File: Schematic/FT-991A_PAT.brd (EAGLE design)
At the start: 44.6 x 59.8 mm, 38 parts, among them Q1 PE4259, Q2 MC78L09, Q3 DG2001, Q5 NCP553, Q7 J310, Q8 BFR193F, X1 IF_IN, X2 SCP_OUT, X3 SDR_OUT

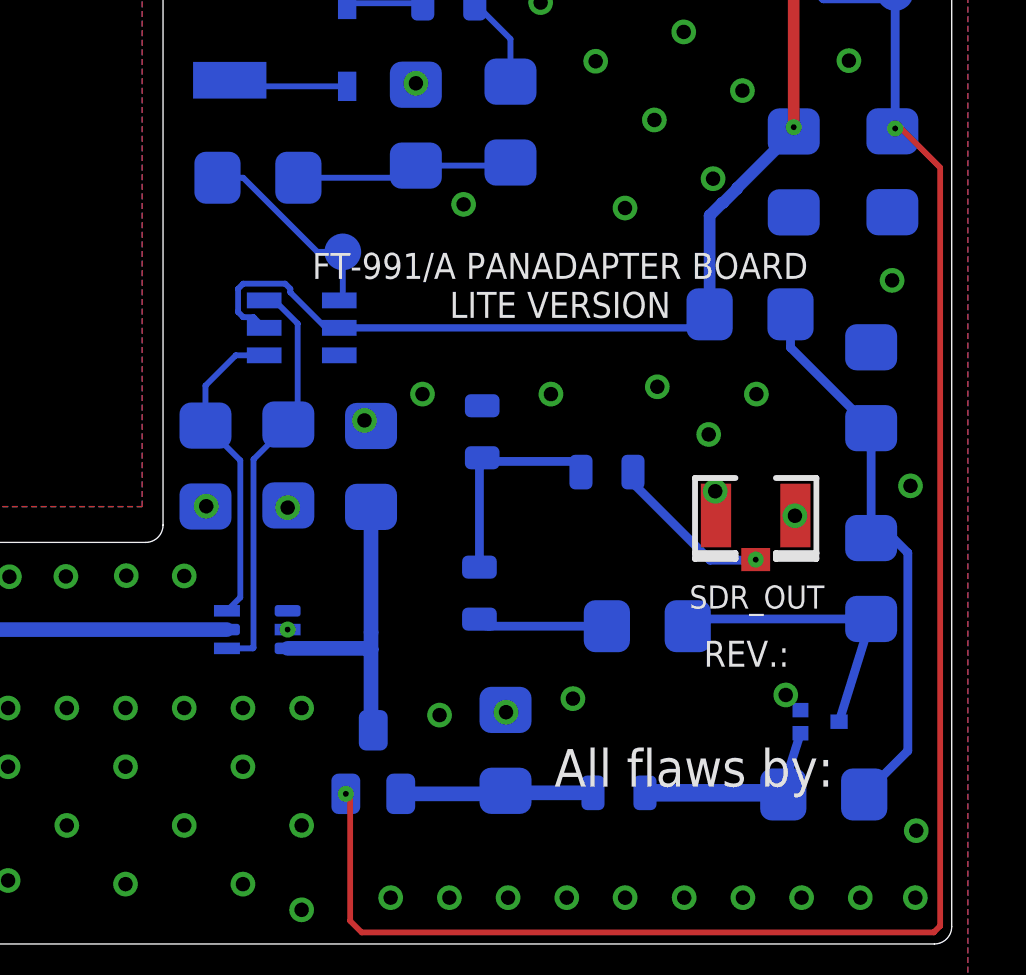
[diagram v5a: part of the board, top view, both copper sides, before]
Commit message: Updating Schematic and Board
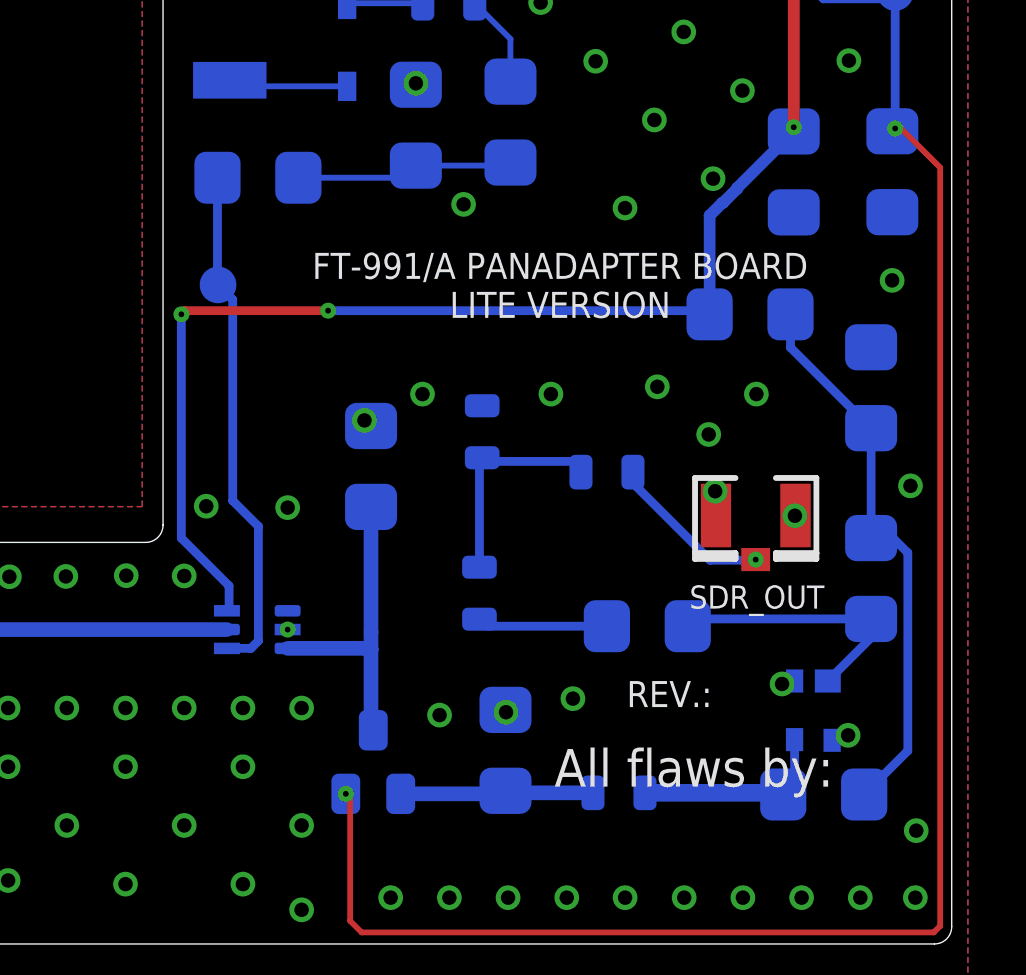
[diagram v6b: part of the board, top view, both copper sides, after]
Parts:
- removed Q3: DG2001, aarf:SOT23-6
- removed R1, R6: 100kΩ, aarf:1206
- Q8: value BFR193F -> BFP460; device aarf:TSFP-3 -> aarf:SOT343R
- moved TP3 4.47 mm to (25.5, 53.2)
- moved Q8 0.46 mm to (46.1, 38.5)
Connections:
- removed net NC: Q1.6, Q3.4, R1.2
- removed net NO: Q1.4, Q3.6, R6.2
- net 3V: now also Q1.6; no longer Q3.2, Q3.5
- net GNDA: now also Q8.1, Q8.3; no longer Q3.3, Q8.2, R1.1, R6.1
- net N$7: now also Q1.4; no longer Q3.1
- net ST2IN: now also Q8.4; no longer Q8.1
- net ST2OUT: now also Q8.2; no longer Q8.3
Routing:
- net NO: track 14.3 -> 0.00 mm
- net NC: track 11.0 -> 0.00 mm
- net 3V: track 43.2 -> 54.0 mm, vias 2 -> 4
- net N$7: track 7.14 -> 17.8 mm
- net ST2OUT: track 10.6 -> 9.62 mm

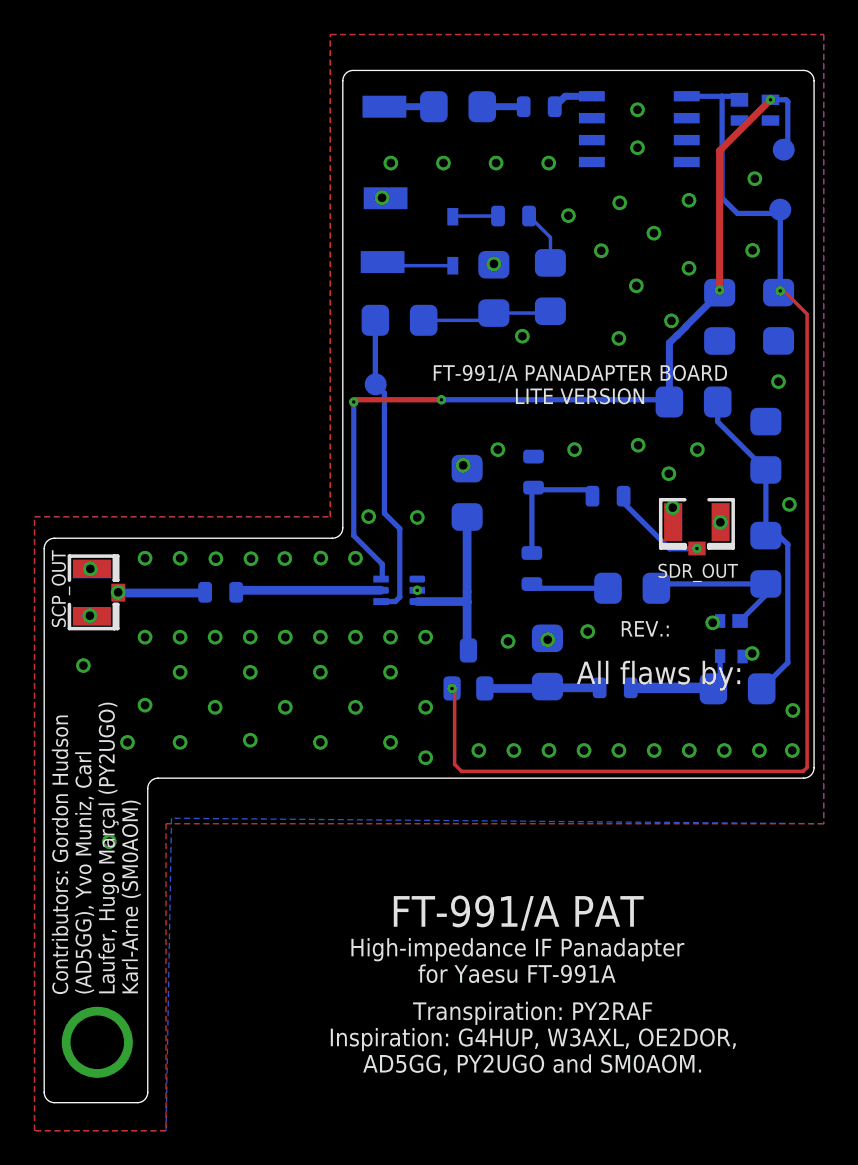
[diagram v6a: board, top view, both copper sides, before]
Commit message: Revision V: Improvements
* Improved BFP460 and NCP553 footprint
* Some routing  and CPW improvements
* Rebasing the library to the latest
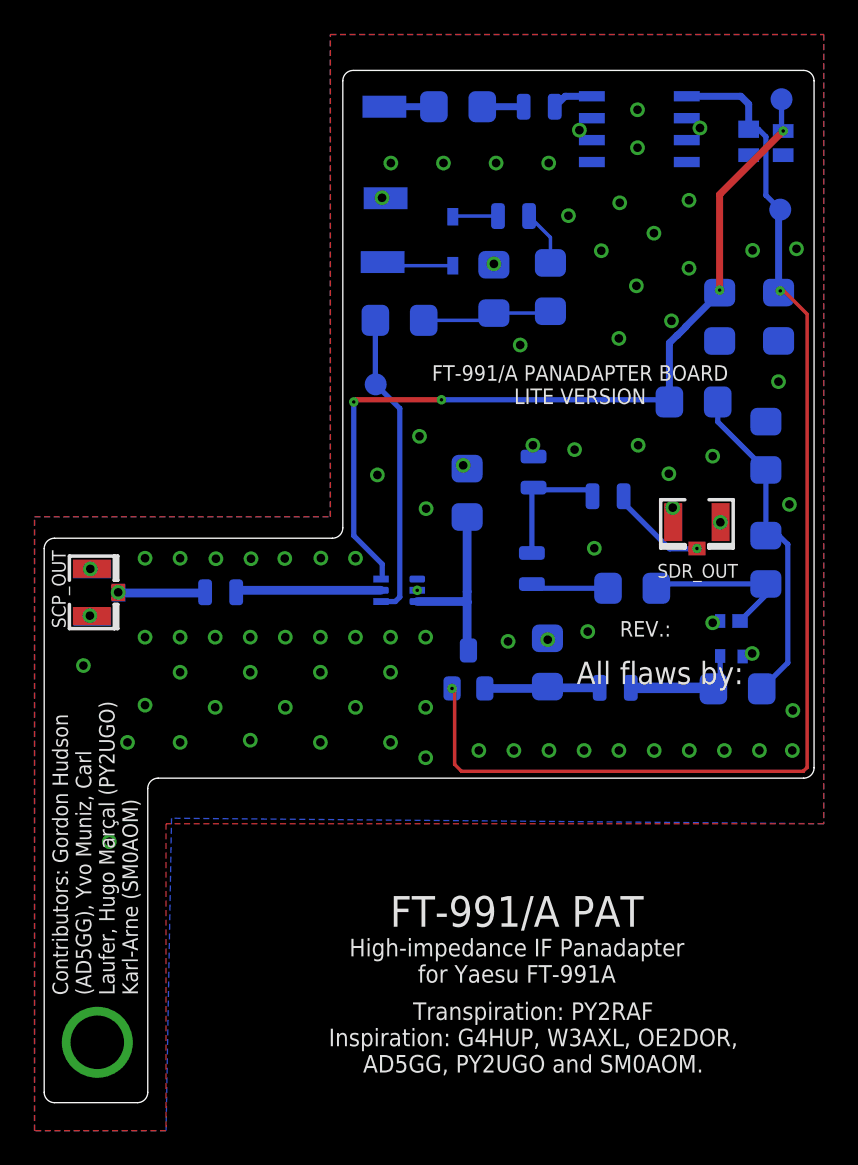
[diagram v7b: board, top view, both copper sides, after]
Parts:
- moved TP2 2.92 mm to (49.0, 69.7)
- moved Q5 2.01 mm to (48.1, 67.2)
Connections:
- net N$18 renamed TX9
- net N$7 renamed SW_FLIP
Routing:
- net 3V: track 54.0 -> 50.7 mm
- net 9V: track 71.5 -> 69.8 mm
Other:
- board text added: "*"
- board text removed: "3x100kΩ"

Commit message: Revision W, Lite Version
* Changed the BFP460 bias network, refactored to the application notes example
* Gemini suggested to put the RF switch **after** the J310 to avoid detuning the IF chain
* Implemented a proper ground-plane co-planar waveguide in the RF stage
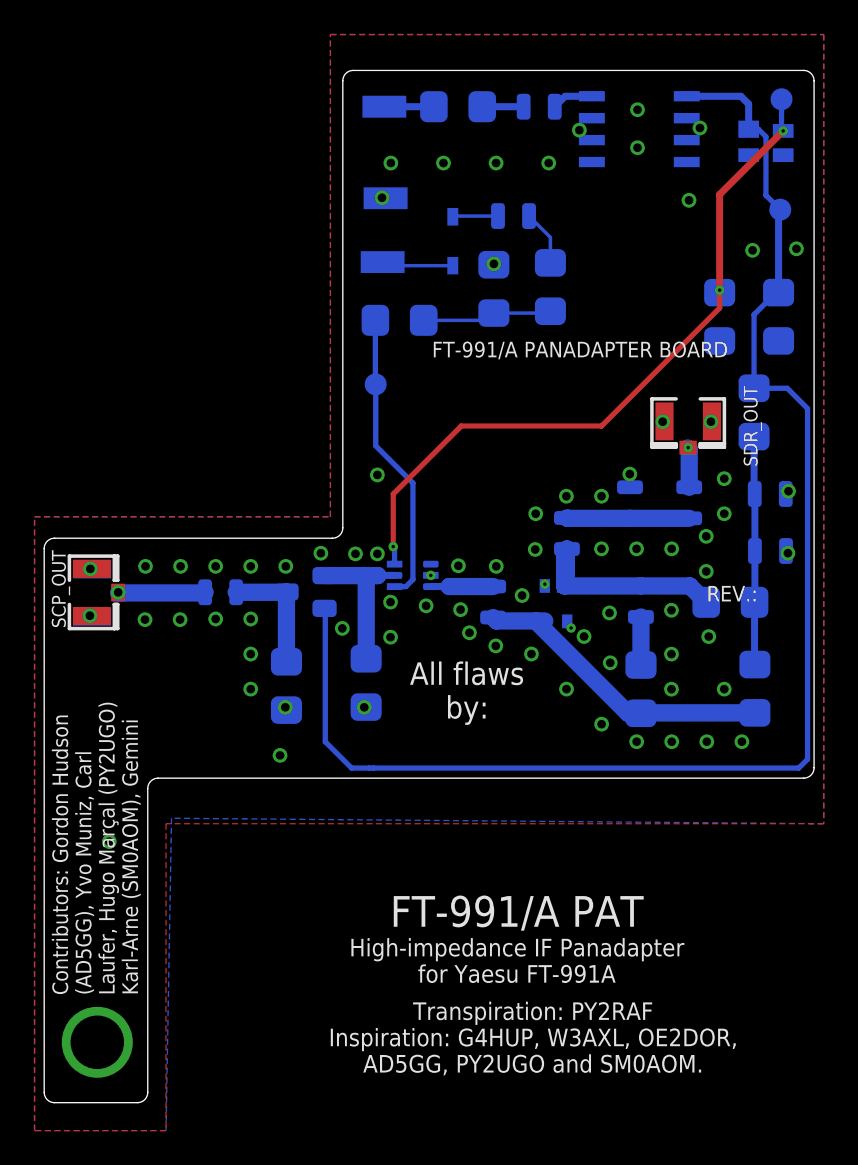
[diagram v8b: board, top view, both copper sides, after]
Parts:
- added C4, C5: 1000pF, aarf:0805
- C1: value 1000pF -> 1.5pF
- C13: value 4.7 nF -> 0.22µF; device aarf:1206 -> aarf:0805
- R11: value 39kΩ -> 300Ω
- R12: value 100Ω -> 82kΩ
- R13: value 27Ω -> 1kΩ
- R14: value 47Ω -> 430Ω
- moved R5 15.3 mm to (20.4, 35.7), turned to 90 degrees
- moved R7 10.6 mm to (25.0, 35.9), turned to 90 degrees
- moved Q7 10.4 mm to (21.5, 41.2), turned to 270 degrees
- moved Q8 10.4 mm to (36.0, 40.5)
- moved C11 8.64 mm to (32.3, 40.6), turned to 270 degrees
- moved R12 7.49 mm to (47.5, 35.6), turned to 90 degrees
- moved C14 5.86 mm to (40.3, 46.4)
- moved X3 5.86 mm to (43.6, 51.1)
- moved R14 5.86 mm to (40.9, 35.6), turned to 90 degrees
- moved R11 5.03 mm to (46.1, 40.6)
- moved L1 4.71 mm to (43.7, 46.4), turned to 90 degrees
- moved R13 3.56 mm to (47.4, 51.6), turned to 270 degrees
- moved C12 2.87 mm to (36.6, 44.6)
- moved C13 2.81 mm to (48.4, 46.9), turned to 180 degrees
- moved Q1 1.17 mm to (27.7, 42.2)
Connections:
- net RAWIN renamed IF-IN
- net ST2M2 renamed LPF-80M
- removed net FB-3V: C13.1, R11.1, R12.1, R13.2
- removed net IFTAP: C1.P$2, Q1.5
- removed net ST1IN: Q1.3, Q7.3, R5.2
- removed net ST1M1: C11.P$1, Q7.1, R7.2
- removed net ST2IN: C11.P$2, Q8.4, R11.2
- removed net ST2M1: C12.P$1, R14.2
- removed net ST2OUT: Q8.2, R12.2, R14.1
- new net AC-FB: C4.P$1, R14.2
- new net COLL-LOAD: C13.P$1, C5.P$1, R11.1, R12.2, R13.2
- new net JFET-IN: C1.P$2, Q7.3, R5.2
- new net JFET-OUT: Q1.5, Q7.1, R7.2
- new net LNA-IN: C11.P$2, Q8.4, R12.1, R14.1
- new net LNA-OUT: C12.P$1, C4.P$2, Q8.2, R11.2
- new net SW-OUT: C11.P$1, Q1.3
- net 3V: no longer R13.1
- net 9V: now also R13.1
- net GNDA: now also C13.P$2, C5.P$2; no longer C13.2
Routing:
- net FB-3V: track 19.4 -> 0.00 mm
- net LNA-IN: track 0.00 -> 18.0 mm
- net COLL-LOAD: track 0.00 -> 13.2 mm
- net 9V: track 69.8 -> 83.0 mm, vias 2 -> 0
- net LNA-OUT: track 0.00 -> 12.3 mm
- net JFET-OUT: track 0.00 -> 12.0 mm
- net ST1IN: track 10.7 -> 0.00 mm
- net ST2OUT: track 9.62 -> 0.00 mm
- net 3V: track 50.7 -> 41.5 mm, vias 4 -> 3
- net IFTAP: track 8.44 -> 0.00 mm
- net JFET-IN: track 0.00 -> 6.96 mm
- net ST2IN: track 6.87 -> 0.00 mm
- net ST1M1: track 6.73 -> 0.00 mm
- net ST2M1: track 4.62 -> 0.00 mm
- net FINAL: track 5.74 -> 2.33 mm
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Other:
- board text added: "Contributors: Gordon Hudson (AD5GG), Yvo Muniz, Carl Laufer, Hugo Marçal (PY2UGO) Karl-Arne (SM0AOM), Gemini"
- board text added: "FT-991/A PANADAPTER BOARD"
- board text removed: "*"
- board text removed: "Contributors: Gordon Hudson (AD5GG), Yvo Muniz, Carl Laufer, Hugo Marçal (PY2UGO) Karl-Arne (SM0AOM)"
- board text removed: "FT-991/A PANADAPTER BOARD LITE VERSION"
